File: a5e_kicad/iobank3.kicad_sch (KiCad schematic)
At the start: 3 parts, among them U7 A5EB013B-B23B

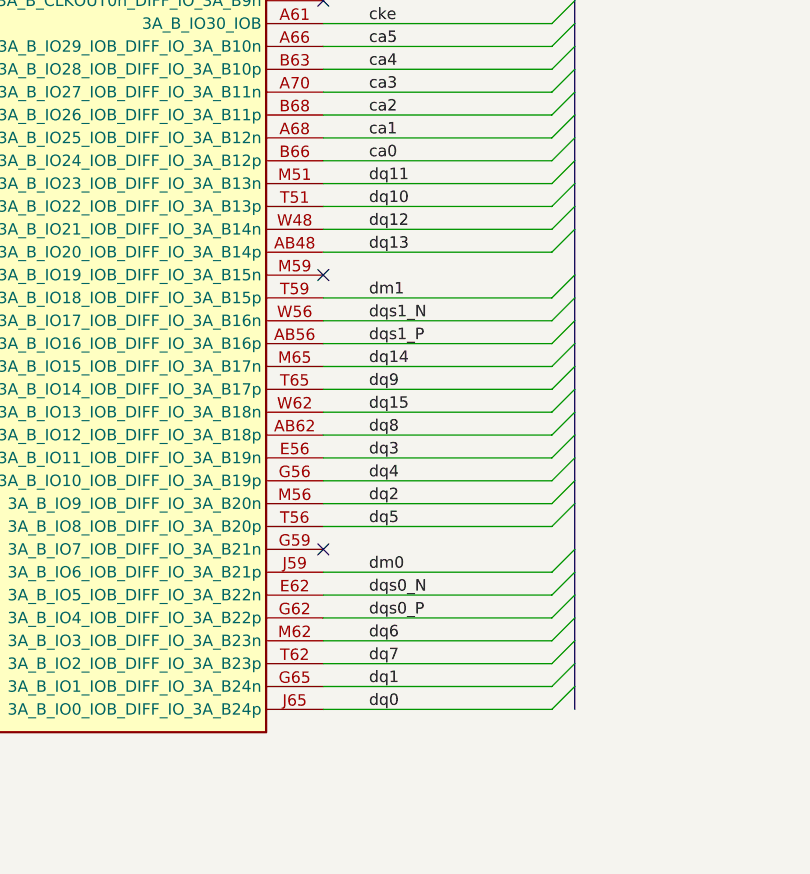
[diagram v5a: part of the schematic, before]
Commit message: LPDDR4: byte 0<->1 swap, CK T under U12, 40/45 ohm route widths and tuning profiles
- Byte swap BL0<->BL1: byte 0 (dq0-7, dqs0, dm0) now on BL1, byte 1 on BL0, each net on its
  partner's lane pin. iobank3 labels and U7 pad nets swapped (22 nets). Quartus fit passes with
  BYTE_SWIZZLE_CH0=1 0 X X X X 3 2 and unchanged per-byte pin strings (src/u7_bank3_pins_bswap.csv).
  dqs0/dqs1 routes trimmed at U7's courtyard (32 segments, 4 vias) to be extended to the new balls.
- CK T on In2: 0.88 mm diagonals to two T-vias on the U12 centre line, all four branches 1.990 mm.
- DRU: lpddr_bga_neckdown diff_pair_gap gets an explicit max (KiCad applied 0.15 mm without one).
- Pre-defined track widths 0.10/0.12/0.15/0.18/0.20 and diff pairs 0.10/0.10, 0.18/0.10, 0.20/0.10.
- Tuning profiles renamed to "40R-45R": 0.18 mm inner (40 ohm), 0.20 mm F/B (~45 ohm), diff gap 0.10.
- Docs: swizzle plan/rules (lane map, package delays, Quartus string), delay matching, next steps.
- DRC 580 violations, 300 unconnected, schematic parity 0 (zones need a refill).
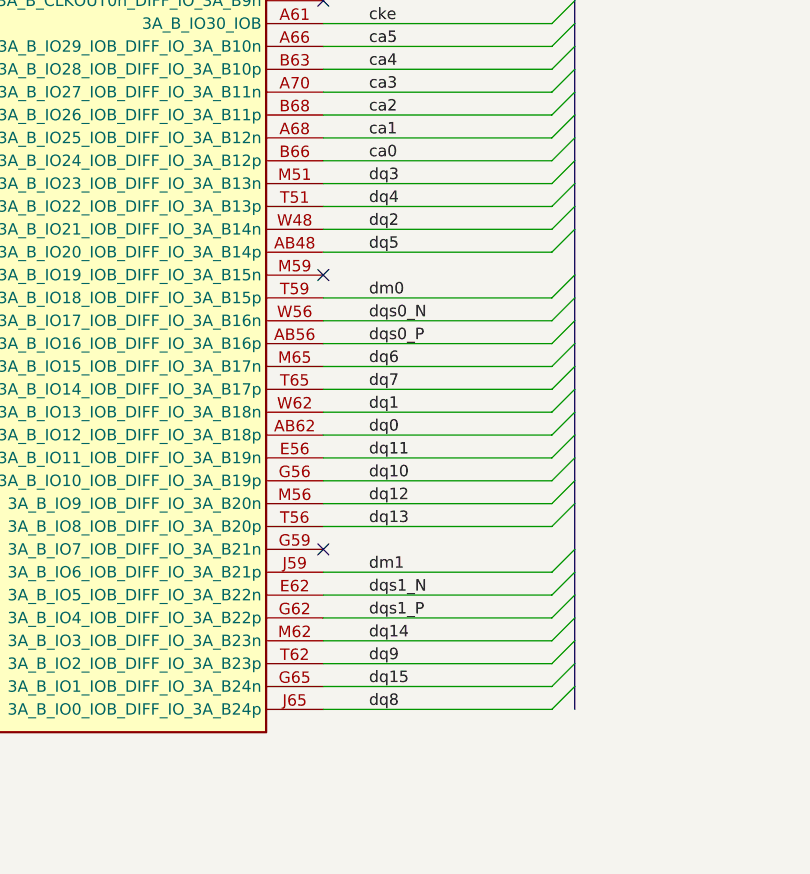
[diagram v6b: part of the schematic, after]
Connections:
- net dm0: now also U7.T59 (3A_B_IO18_IOB_DIFF_IO_3A_B15p); no longer U7.J59 (3A_B_IO6_IOB_DIFF_IO_3A_B21p)
- net dm1: now also U7.J59 (3A_B_IO6_IOB_DIFF_IO_3A_B21p); no longer U7.T59 (3A_B_IO18_IOB_DIFF_IO_3A_B15p)
- net dq0: now also U7.AB62 (3A_B_IO12_IOB_DIFF_IO_3A_B18p); no longer U7.J65 (3A_B_IO0_IOB_DIFF_IO_3A_B24p)
- net dq1: now also U7.W62 (3A_B_IO13_IOB_DIFF_IO_3A_B18n); no longer U7.G65 (3A_B_IO1_IOB_DIFF_IO_3A_B24n)
- net dq10: now also U7.G56 (3A_B_IO10_IOB_DIFF_IO_3A_B19p); no longer U7.T51 (3A_B_IO22_IOB_DIFF_IO_3A_B13p)
- net dq11: now also U7.E56 (3A_B_IO11_IOB_DIFF_IO_3A_B19n); no longer U7.M51 (3A_B_IO23_IOB_DIFF_IO_3A_B13n)
- net dq12: now also U7.M56 (3A_B_IO9_IOB_DIFF_IO_3A_B20n); no longer U7.W48 (3A_B_IO21_IOB_DIFF_IO_3A_B14n)
- net dq13: now also U7.T56 (3A_B_IO8_IOB_DIFF_IO_3A_B20p); no longer U7.AB48 (3A_B_IO20_IOB_DIFF_IO_3A_B14p)
- net dq14: now also U7.M62 (3A_B_IO3_IOB_DIFF_IO_3A_B23n); no longer U7.M65 (3A_B_IO15_IOB_DIFF_IO_3A_B17n)
- net dq15: now also U7.G65 (3A_B_IO1_IOB_DIFF_IO_3A_B24n); no longer U7.W62 (3A_B_IO13_IOB_DIFF_IO_3A_B18n)
- net dq2: now also U7.W48 (3A_B_IO21_IOB_DIFF_IO_3A_B14n); no longer U7.M56 (3A_B_IO9_IOB_DIFF_IO_3A_B20n)
- net dq3: now also U7.M51 (3A_B_IO23_IOB_DIFF_IO_3A_B13n); no longer U7.E56 (3A_B_IO11_IOB_DIFF_IO_3A_B19n)
- net dq4: now also U7.T51 (3A_B_IO22_IOB_DIFF_IO_3A_B13p); no longer U7.G56 (3A_B_IO10_IOB_DIFF_IO_3A_B19p)
- net dq5: now also U7.AB48 (3A_B_IO20_IOB_DIFF_IO_3A_B14p); no longer U7.T56 (3A_B_IO8_IOB_DIFF_IO_3A_B20p)
- net dq6: now also U7.M65 (3A_B_IO15_IOB_DIFF_IO_3A_B17n); no longer U7.M62 (3A_B_IO3_IOB_DIFF_IO_3A_B23n)
- net dq7: now also U7.T65 (3A_B_IO14_IOB_DIFF_IO_3A_B17p); no longer U7.T62 (3A_B_IO2_IOB_DIFF_IO_3A_B23p)
- net dq8: now also U7.J65 (3A_B_IO0_IOB_DIFF_IO_3A_B24p); no longer U7.AB62 (3A_B_IO12_IOB_DIFF_IO_3A_B18p)
- net dq9: now also U7.T62 (3A_B_IO2_IOB_DIFF_IO_3A_B23p); no longer U7.T65 (3A_B_IO14_IOB_DIFF_IO_3A_B17p)
- net dqs0_N: now also U7.W56 (3A_B_IO17_IOB_DIFF_IO_3A_B16n); no longer U7.E62 (3A_B_IO5_IOB_DIFF_IO_3A_B22n)
- net dqs0_P: now also U7.AB56 (3A_B_IO16_IOB_DIFF_IO_3A_B16p); no longer U7.G62 (3A_B_IO4_IOB_DIFF_IO_3A_B22p)
- net dqs1_N: now also U7.E62 (3A_B_IO5_IOB_DIFF_IO_3A_B22n); no longer U7.W56 (3A_B_IO17_IOB_DIFF_IO_3A_B16n)
- net dqs1_P: now also U7.G62 (3A_B_IO4_IOB_DIFF_IO_3A_B22p); no longer U7.AB56 (3A_B_IO16_IOB_DIFF_IO_3A_B16p)
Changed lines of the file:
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@@
 		)
 	)
-	(label "dqs1_N"
+	(label "dqs0_N"
 		(at 208.28 116.84 0)
 		(effects
@@
 		)
 	)
-	(label "dq9"
+	(label "dq7"
 		(at 208.28 124.46 0)
 		(effects
@@
 		)
 	)
-	(label "dq10"
+	(label "dq4"
 		(at 208.28 104.14 0)
 		(effects
@@
 		)
 	)
-	(label "dq8"
+	(label "dq0"
 		(at 208.28 129.54 0)
 		(effects
@@
 		)
 	)
-	(label "dm0"
+	(label "dm1"
 		(at 208.28 144.78 0)
 		(effects
@@
 		)
 	)
-	(label "dq2"
+	(label "dq12"
 		(at 208.28 137.16 0)
 		(effects
@@
 		)
 	)
-	(label "dq13"
+	(label "dq5"
 		(at 208.28 109.22 0)
 		(effects
@@
 		)
 	)
-	(label "dq0"
+	(label "dq8"
 		(at 208.28 160.02 0)
 		(effects
@@
 		)
 	)
+	(label "dq11"
+		(at 208.28 132.08 0)
+		(effects
+			(font
+				(size 1.27 1.27)
+			)
+			(justify left bottom)
+		)
+	)
 	(label "dq3"
-		(at 208.28 132.08 0)
-		(effects
-			(font
-				(size 1.27 1.27)
-			)
-			(justify left bottom)
-		)
-	)
-	(label "dq11"
 		(at 208.28 101.6 0)
 		(effects
@@
 		)
 	)
-	(label "dq7"
+	(label "dq9"
 		(at 208.28 154.94 0)
 		(effects
@@
 		)
 	)
-	(label "dqs0_P"
+	(label "dqs1_P"
 		(at 208.28 149.86 0)
 		(effects
@@
 		)
 	)
-	(label "dq1"
+	(label "dq15"
 		(at 208.28 157.48 0)
 		(effects
@@
 		)
 	)
-	(label "dq6"
+	(label "dq14"
 		(at 208.28 152.4 0)
 		(effects
@@
 		)
 	)
-	(label "dq14"
+	(label "dq6"
 		(at 208.28 121.92 0)
 		(effects
@@
 		)
 	)
-	(label "dq5"
+	(label "dq13"
 		(at 208.28 139.7 0)
 		(effects
@@
 		)
 	)
-	(label "dq4"
+	(label "dq10"
 		(at 208.28 134.62 0)
 		(effects
@@
 		)
 	)
-	(label "dm1"
+	(label "dm0"
 		(at 208.28 114.3 0)
 		(effects
@@
 		)
 	)
-	(label "dqs1_P"
+	(label "dqs0_P"
 		(at 208.28 119.38 0)
 		(effects
@@
 		)
 	)
-	(label "dq12"
+	(label "dq2"
 		(at 208.28 106.68 0)
 		(effects
@@
 		)
 	)
-	(label "dq15"
+	(label "dq1"
 		(at 208.28 127 0)
 		(effects
@@
 		)
 	)
-	(label "dqs0_N"
+	(label "dqs1_N"
 		(at 208.28 147.32 0)
 		(effects

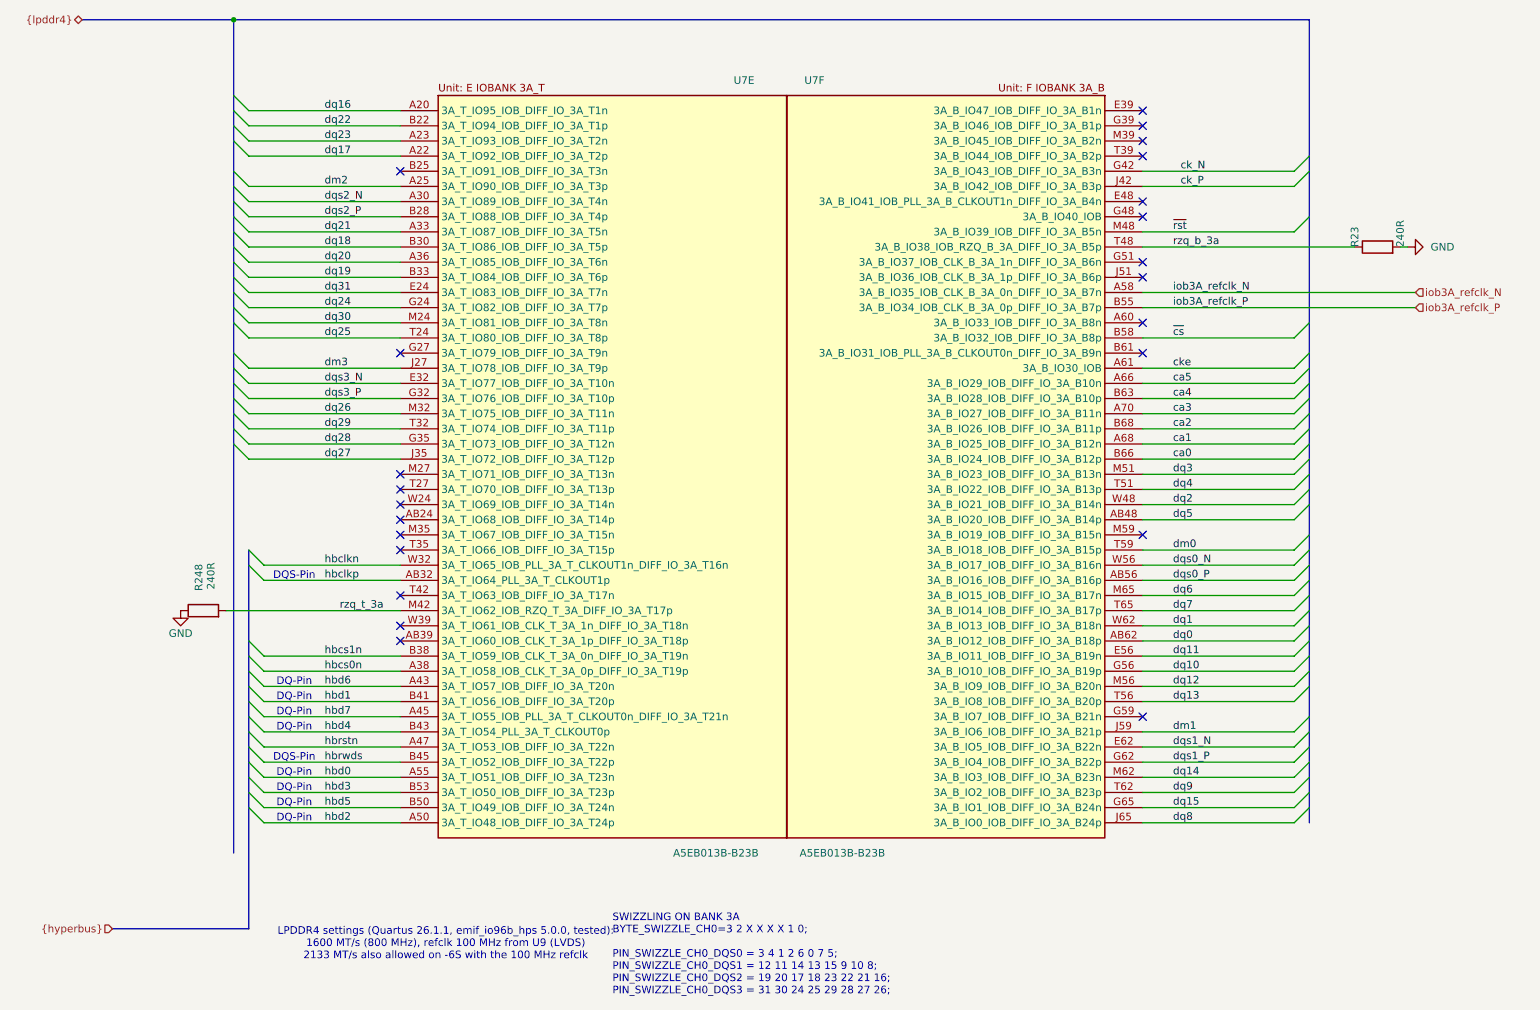
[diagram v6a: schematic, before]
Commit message: LPDDR4 routing in progress: in-lane DQ swizzle (bytes 0, 2, 3), schematic and PCB
- iobank3: in-lane DQ swaps in byte 0 (BL1 dq3-dq6), byte 2 (BL7 dq17-dq23) and
  byte 3 (BL6 dq25/26/28/31); byte swizzle unchanged (1 0 X X X X 3 2).
- PCB: routing of bytes 0-3 in progress (DQ on F.Cu / In5, DQS/DM on In2); U7/U12
  pad nets match the schematic.
- Quartus test build (varA_sch1028) passes synthesis, fitter and timing with
  PIN_SWIZZLE DQS0=0 1 7 5 3 2 6 4, DQS1=8 15 9 14 13 12 10 11,
  DQS2=20 19 21 18 22 17 23 16, DQS3=27 26 29 28 31 30 24 25.
- Swizzle docs: lane map, Quartus strings, package delays per net updated; the
  swizzle is marked work in progress (more swaps while the other channel is routed).
- Other schematic sheet edits as in the working tree (bank 6A at 3.3 V, CE19 no
  longer takes sdm_clk25, etc.).
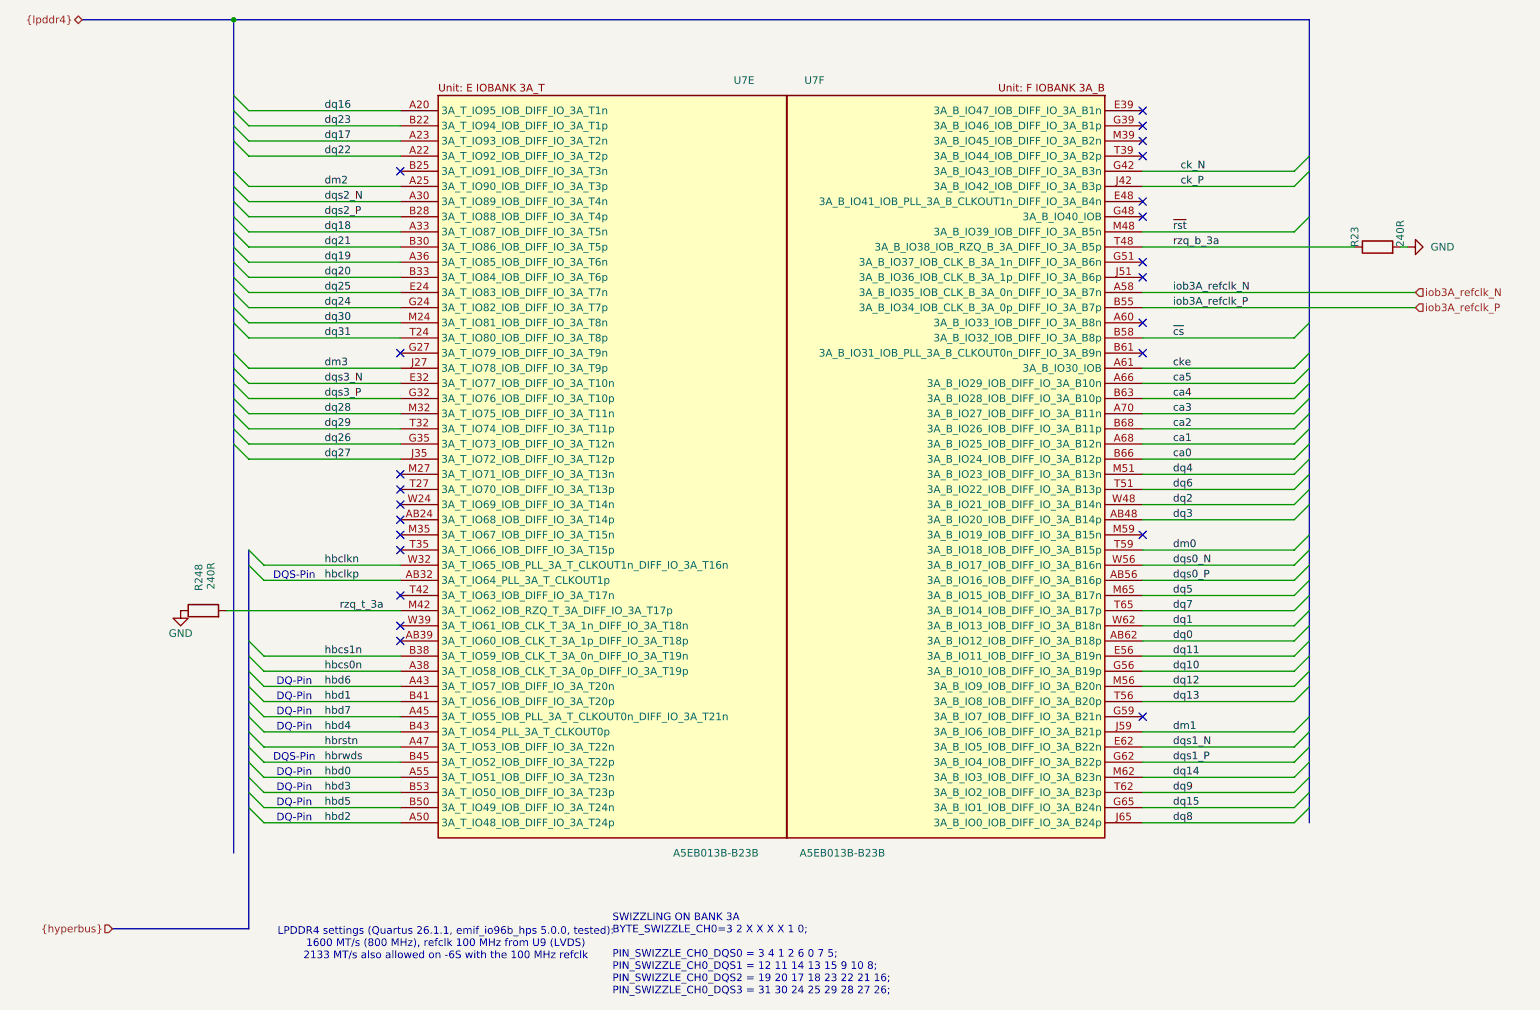
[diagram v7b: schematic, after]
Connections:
- net dq17: now also U7.A23 (3A_T_IO93_IOB_DIFF_IO_3A_T2n); no longer U7.A22 (3A_T_IO92_IOB_DIFF_IO_3A_T2p)
- net dq18: now also U7.A33 (3A_T_IO87_IOB_DIFF_IO_3A_T5n); no longer U7.B30 (3A_T_IO86_IOB_DIFF_IO_3A_T5p)
- net dq19: now also U7.A36 (3A_T_IO85_IOB_DIFF_IO_3A_T6n); no longer U7.B33 (3A_T_IO84_IOB_DIFF_IO_3A_T6p)
- net dq20: now also U7.B33 (3A_T_IO84_IOB_DIFF_IO_3A_T6p); no longer U7.A36 (3A_T_IO85_IOB_DIFF_IO_3A_T6n)
- net dq21: now also U7.B30 (3A_T_IO86_IOB_DIFF_IO_3A_T5p); no longer U7.A33 (3A_T_IO87_IOB_DIFF_IO_3A_T5n)
- net dq22: now also U7.A22 (3A_T_IO92_IOB_DIFF_IO_3A_T2p); no longer U7.B22 (3A_T_IO94_IOB_DIFF_IO_3A_T1p)
- net dq23: now also U7.B22 (3A_T_IO94_IOB_DIFF_IO_3A_T1p); no longer U7.A23 (3A_T_IO93_IOB_DIFF_IO_3A_T2n)
- net dq25: now also U7.E24 (3A_T_IO83_IOB_DIFF_IO_3A_T7n); no longer U7.T24 (3A_T_IO80_IOB_DIFF_IO_3A_T8p)
- net dq26: now also U7.G35 (3A_T_IO73_IOB_DIFF_IO_3A_T12n); no longer U7.M32 (3A_T_IO75_IOB_DIFF_IO_3A_T11n)
- net dq28: now also U7.M32 (3A_T_IO75_IOB_DIFF_IO_3A_T11n); no longer U7.G35 (3A_T_IO73_IOB_DIFF_IO_3A_T12n)
- net dq3: now also U7.AB48 (3A_B_IO20_IOB_DIFF_IO_3A_B14p); no longer U7.M51 (3A_B_IO23_IOB_DIFF_IO_3A_B13n)
- net dq31: now also U7.T24 (3A_T_IO80_IOB_DIFF_IO_3A_T8p); no longer U7.E24 (3A_T_IO83_IOB_DIFF_IO_3A_T7n)
- net dq4: now also U7.M51 (3A_B_IO23_IOB_DIFF_IO_3A_B13n); no longer U7.T51 (3A_B_IO22_IOB_DIFF_IO_3A_B13p)
- net dq5: now also U7.M65 (3A_B_IO15_IOB_DIFF_IO_3A_B17n); no longer U7.AB48 (3A_B_IO20_IOB_DIFF_IO_3A_B14p)
- net dq6: now also U7.T51 (3A_B_IO22_IOB_DIFF_IO_3A_B13p); no longer U7.M65 (3A_B_IO15_IOB_DIFF_IO_3A_B17n)
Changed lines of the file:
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@@
 		)
 	)
-	(label "dq31"
+	(label "dq25"
 		(at 66.04 71.12 0)
 		(effects
@@
 		)
 	)
-	(label "dq4"
+	(label "dq6"
 		(at 208.28 104.14 0)
 		(effects
@@
 		)
 	)
-	(label "dq21"
+	(label "dq18"
 		(at 66.04 60.96 0)
 		(effects
@@
 		)
 	)
-	(label "dq5"
+	(label "dq3"
 		(at 208.28 109.22 0)
 		(effects
@@
 		)
 	)
-	(label "dq3"
+	(label "dq4"
 		(at 208.28 101.6 0)
 		(effects
@@
 		)
 	)
-	(label "dq25"
+	(label "dq31"
 		(at 66.04 78.74 0)
 		(effects
@@
 		)
 	)
-	(label "dq20"
+	(label "dq19"
 		(at 66.04 66.04 0)
 		(effects
@@
 		)
 	)
-	(label "dq6"
+	(label "dq5"
 		(at 208.28 121.92 0)
 		(effects
@@
 		)
 	)
-	(label "dq22"
+	(label "dq23"
 		(at 66.04 43.18 0)
 		(effects
@@
 		)
 	)
-	(label "dq28"
+	(label "dq26"
 		(at 66.04 96.52 0)
 		(effects
@@
 		)
 	)
-	(label "dq18"
+	(label "dq21"
 		(at 66.04 63.5 0)
 		(effects
@@
 		)
 	)
-	(label "dq19"
+	(label "dq20"
 		(at 66.04 68.58 0)
 		(effects
@@
 		)
 	)
-	(label "dq26"
+	(label "dq28"
 		(at 66.04 91.44 0)
 		(effects
@@
 		)
 	)
-	(label "dq23"
+	(label "dq17"
 		(at 66.04 45.72 0)
 		(effects
@@
 		)
 	)
-	(label "dq17"
+	(label "dq22"
 		(at 66.04 48.26 0)
 		(effects
@@
 			)
 		)
-		(property "LCSC" "C25094"
-			(at 242.57 65.278 90)
+		(property "Datasheet" ""
+			(at 242.57 63.5 0)
 			(hide yes)
 			(show_name no)
@@
 			)
 		)
-		(property "Datasheet" ""
+		(property "Description" "Resistor"
 			(at 242.57 63.5 0)
 			(hide yes)
@@
 			)
 		)
-		(property "Description" "Resistor"
-			(at 242.57 63.5 0)
+		(property "LCSC" "C25094"
+			(at 242.57 65.278 90)
 			(hide yes)
 			(show_name no)
@@
 			)
 		)
-		(property "LCSC" "C25094"
+		(property "Datasheet" "~"
 			(at 45.72 124.46 90)
 			(hide yes)
@@
 			)
 		)
-		(property "Datasheet" "~"
+		(property "Description" "Resistor"
 			(at 45.72 124.46 90)
 			(hide yes)
@@
 			)
 		)
-		(property "Description" "Resistor"
+		(property "LCSC" "C25094"
 			(at 45.72 124.46 90)
 			(hide yes)
